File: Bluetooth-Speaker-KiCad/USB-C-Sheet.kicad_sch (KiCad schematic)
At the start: 2 parts, among them J1 USB_C_Receptacle_USB2.0_14P, U2 TPD4E02B04DQA

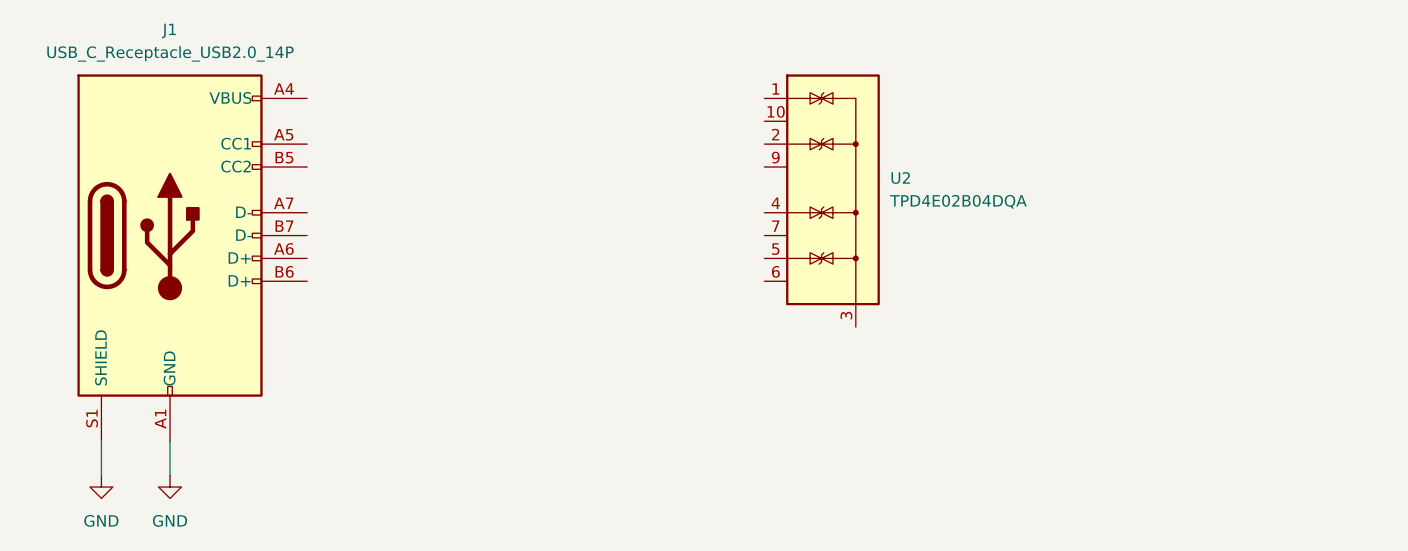
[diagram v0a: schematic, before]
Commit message: USB Connections
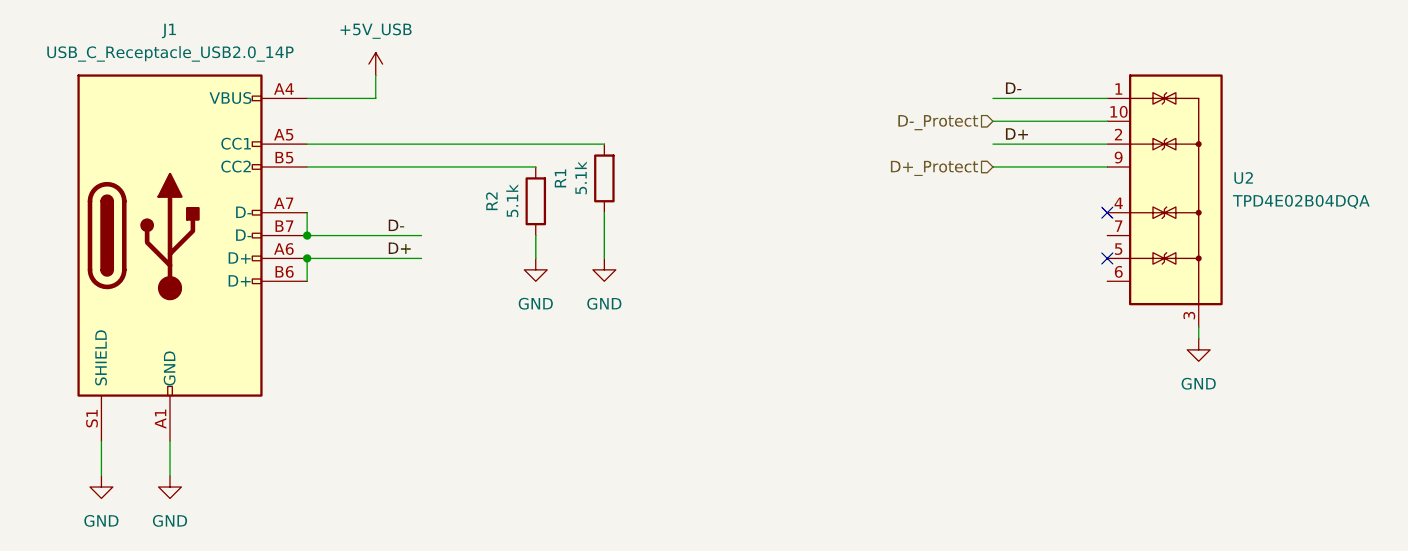
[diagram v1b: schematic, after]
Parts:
- added R1, R2: 5.1k, Resistor_SMD:R_0603_1608Metric_Pad0.98x0.95mm_HandSolder, symbol Device:R
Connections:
- net GND: now also U2.3 (G), U2.8 (G), R1.1, R2.1
- net D-: now reaches U2.1 (IO1)
- net D-: now also J1.A7 (D-), J1.B7 (D-)
- net D-_Protect: now reaches U2.10 (NC)
- net D+: now reaches U2.2 (IO2)
- net D+: now also J1.A6 (D+), J1.B6 (D+)
- net D+_Protect: now reaches U2.9 (NC)
- net +5V_USB: now reaches J1.A4 (VBUS), J1.A9 (VBUS), J1.B4 (VBUS), J1.B9 (VBUS)
- net at J1.A5 (CC1): now also R1.2
- net at J1.B5 (CC2): now also R2.2
- no-connect marks 0 -> 2
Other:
- moved on the sheet: U2
